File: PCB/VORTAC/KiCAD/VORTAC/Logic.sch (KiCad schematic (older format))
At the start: 46 parts, among them IC1 TMC2209-LA-T, Q1 WSD4066DN, Q3 WSD4066DN, Q4 Q_NMOS_GSD, Q5 Q_NPN_BEC, Q6 Q_PNP_BEC, Q7 Q_NMOS_GSD, Q8 Q_PMOS_GSD, U2 ADXL343

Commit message: progress
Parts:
- removed C10: 100uF/35V, symbol Device:CP
- removed IC1: TMC2209-LA-T, ToolChanger:tmc_2209_package, symbol ToolChanger:TMC2209-LA-T
- removed R16, R17: ???, symbol Device:R_Small
- removed R18, R21: 22k, symbol Device:R_Small
- removed R19: 1K, symbol Device:R_Small
- removed R20: 22K, symbol Device:R_Small
- removed U2: ADXL343, Package_LGA:LGA-14_3x5mm_P0.8mm_LayoutBorder1x6y, symbol Sensor_Motion:ADXL343
- added 10uH1, 10uH2: L, ToolChanger:L_Sunlord_MWSA0518_5.4x5.2mm, symbol Device:L
- added C10: 360pF, Capacitor_SMD:C_0603_1608Metric, symbol Device:C_Small
- added C11: 0.1uF, Capacitor_SMD:C_0603_1608Metric, symbol Device:C_Small
- added C12: 3.3nF, Capacitor_SMD:C_0603_1608Metric, symbol Device:C_Small
- added C13: 30pF, Capacitor_SMD:C_0603_1608Metric, symbol Device:C_Small
- added C14: 56pF, Capacitor_SMD:C_0603_1608Metric, symbol Device:C_Small
- added C15, C17, C19: 47uF, Capacitor_SMD:C_1206_3216Metric, symbol Device:C_Small
- added C16, C18, C20: 47uF, Capacitor_SMD:C_0805_2012Metric, symbol Device:C_Small
- added R22: 36.5k, Resistor_SMD:R_0402_1005Metric, symbol Device:R_Small
- added R23: 10k, Resistor_SMD:R_0402_1005Metric, symbol Device:R_Small
- added R24, R25: 95k, Resistor_SMD:R_0402_1005Metric, symbol Device:R_Small
- added R26, R28: 100k, Resistor_SMD:R_0402_1005Metric, symbol Device:R_Small
- added R27: 7.15k, Resistor_SMD:R_0402_1005Metric, symbol Device:R_Small
- added R29: 19.1k, Resistor_SMD:R_0402_1005Metric, symbol Device:R_Small
- added U1: TLV73333PDBV, Package_TO_SOT_SMD:SOT-23-5, symbol Regulator_Linear:TLV73333PDBV
- added U3, U4: TPS54335ADRCR, Package_SON:VSON-10-1EP_3x3mm_P0.5mm_EP1.65x2.4mm_ThermalVias, symbol ToolChanger:TPS54335ADRCR
- C1: renamed from C2; value C_Small -> 10uF 50V; footprint (none) -> Resistor_SMD:R_0603_1608Metric
- C3: value 2.2μ/6.3V -> 1uF; footprint (none) -> Capacitor_SMD:C_0603_1608Metric; LCSC (none) -> C152910
- C4: value 100n/16V -> 10uF; footprint (none) -> Capacitor_SMD:C_1206_3216Metric; LCSC (none) -> C89632
- C5: value 100n -> 10uF; footprint (none) -> Capacitor_SMD:C_1206_3216Metric; LCSC (none) -> C89632
- C6: value 22n/50V -> 0.1uF; footprint (none) -> Capacitor_SMD:C_0603_1608Metric; LCSC (none) -> C1591
- C7: value 100nV -> 0.1uF; footprint (none) -> Capacitor_SMD:C_0603_1608Metric; LCSC (none) -> C1591
- C8: value 100nV -> 1uF; footprint (none) -> Capacitor_SMD:C_0603_1608Metric; LCSC (none) -> C152910
- C9: value C_Small -> 0.1uF; footprint (none) -> Capacitor_SMD:C_0603_1608Metric; LCSC (none) -> C1591
- renumbered C1 to C2, Q8 to Q1, Q7 to Q2, Q1 to Q5, Q5 to Q7, R6 to R10, R14 to R11, R10 to R14, R11 to R15, R15 to R16, R24 to R17, R25 to R18, R26 to R19, R27 to R20, R9 to R21, R22 to R5, R23 to R6, R5 to R9
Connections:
- net TMC_VS is gone; now on net GND: C4.2, C7.2, C8.2
- net 3.3V: now also C8.1, U1.5 (OUT); no longer C5.1, C9.1
- net GND: now also C6.2, C10.2, C12.2, C13.2, C14.2, C15.2, C16.2, C17.2, C18.2, C19.2, C20.2, R24.1, R25.1, R27.2, R29.2, U1.2 (GND), U3.11 (THRM), U3.3 (GND), U3.4 (GND), U3.5 (GND), U4.11 (THRM), U4.3 (GND), U4.4 (GND), U4.5 (GND); no longer C7.1, C8.1, C9.2
- net V_IN: now also C4.1, C5.1, C6.1, C7.1, U3.1 (VIN), U4.1 (VIN)
- net 5V: now reaches C3.1
- net 5V: now also 10uH2.2, C16.1, C18.1, C20.1, R28.1, U1.1 (IN), U1.3 (EN)
- net THERM_1 renamed THERM_1_OUT
- net USBH_DRAIN renamed HOST_USB_DRAIN
- new net: R24.2, U3.10 (RT)
- new net: 10uH1.1, C9.1, U3.2 (PH)
- new net: C9.2, U3.9 (BOOT)
- new net: C13.1, R22.1
- new net: C10.1, R22.2, U3.7 (COMP)
- new net: R26.2, R27.1, U3.6 (VSENSE)
- new net: R25.2, U4.10 (RT)
- new net: 10uH2.1, C11.1, U4.2 (PH)
- new net: C11.2, U4.9 (BOOT)
- new net: C14.1, R23.1
- new net: C12.1, R23.2, U4.7 (COMP)
- new net: R28.2, R29.1, U4.6 (VSENSE)
- new net 12V: 10uH1.2, C15.1, C17.1, C19.1, R26.1
- no-connect marks 5 -> 2
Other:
- note added: "12V DC-DC Converter\n(capable of min 2A)"
- note added: "5V DC-DC Converter\n(capable of min 2.5A)"
- note added: "R2 = 0.8 / (VOUT-0.8) * 100K\nR2 = 19.047 >> 19.1K\n\nVOUT = 0.8 * R1/R2 + 0.8\nVOUT = 4.98V\n\nRT = 55300/FSW^-1.025\nRT(500 kHz) = 94.68K"
- note added: "R2 = 0.8 / (VOUT-0.8) * 100K\nR2 = 7.142 >> 7.15K\n\nVOUT = 0.8 * R1/R2 + 0.8\nVOUT =11.98V\n\nRT = 55300/FSW^-1.025\nRT(500 kHz) = 94.68K"
- note removed: "ADXL_345"
- note removed: "TMC2209"
- note removed: "TODO: This needs to be changed to ADXL345"
- note removed: "TODO: add output protection"
- moved on the sheet: C1, C2, Q3A, Q3B, Q4, Q5A, Q5B, R10, R11, R12, R13, R14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

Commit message: progress
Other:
- note added: "3.3V Linear Voltage Regulator\n(300mA for internal use only)"
- note added: "HEATER MOSFET - IRF8736TRPBF"
- note added: "THERMISTOR PASSIVES"
- note removed: "HEATER MOSFET - Infineon Technologies IRF8736TRPBF"
- moved on the sheet: 10uH1, 10uH2, C10, C11, C12, C13, C14, C15, C16, C17, C18, C19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

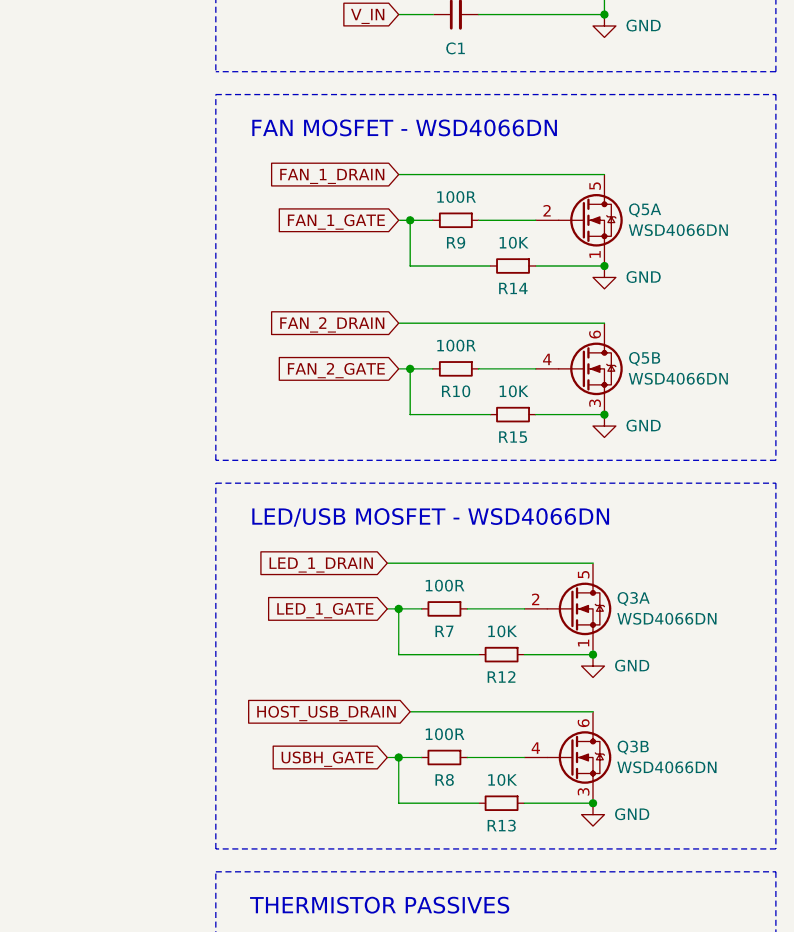
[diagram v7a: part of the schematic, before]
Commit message: Layouting & Footprints
-Improved Thermal Footprint Conductivity
-Improved Component Spacing
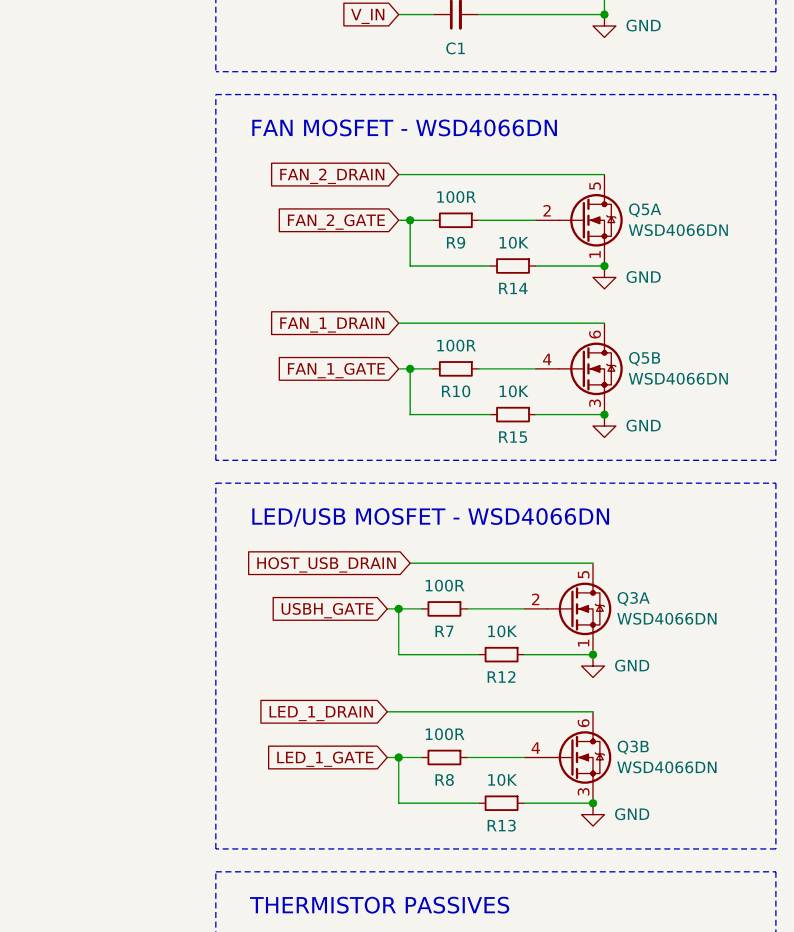
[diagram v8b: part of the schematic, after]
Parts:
- C2: footprint Capacitor_SMD:C_0402_1005Metric_Pad0.74x0.62mm_HandSolder -> Capacitor_SMD:C_0402_1005Metric
- Q3, Q5: footprint ToolChanger:WSD4066DN -> ToolChanger:WSD4066DN_ThermalPad
- U3, U4: footprint Package_SON:VSON-10-1EP_3x3mm_P0.5mm_EP1.65x2.4mm_ThermalVias -> ToolChanger:VSON-10-1EP_3x3mm_P0.5mm_EP1.65x2.4mm_ThermalVias
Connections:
- net FAN_1_DRAIN: now also Q5.6 (D2); no longer Q5.5 (D2)
- net FAN_1_GATE: now also R10.2, R15.2; no longer R14.2, R9.2
- net FAN_2_DRAIN: now also Q5.5 (D2); no longer Q5.6 (D2)
- net FAN_2_GATE: now also R14.2, R9.2; no longer R10.2, R15.2
- net HOST_USB_DRAIN: now also Q3.5 (D2); no longer Q3.6 (D2)
- net LED_1_DRAIN: now also Q3.6 (D2); no longer Q3.5 (D2)
- net LED_1_GATE: now also R13.2, R8.2; no longer R12.2, R7.2
- net USBH_GATE: now also R12.2, R7.2; no longer R13.2, R8.2
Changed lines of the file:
@@
 F 0 "Q5" H 10404 3246 50  0000 L CNN
 F 1 "WSD4066DN" H 10404 3155 50  0000 L CNN
-F 2 "ToolChanger:WSD4066DN" H 10400 3125 50  0001 L CIN
+F 2 "ToolChanger:WSD4066DN_ThermalPad" H 10400 3125 50  0001 L CIN
 F 3 "https://www.lcsc.com/product-detail/MOSFETs_Winsok-Semicon-WSD4066DN_C377861.html" H 10200 3200 50  0001 L CNN
 F 4 "C377861" H 10200 3200 50  0001 C CNN "LCSC"
@@
 	1    0    0    -1
 $EndComp
-Text GLabel 9400 3000 0    50   Input ~ 0
+Text GLabel 9400 2350 0    50   Input ~ 0
 FAN_2_DRAIN
-Text GLabel 9400 3200 0    50   Input ~ 0
+Text GLabel 9400 2550 0    50   Input ~ 0
 FAN_2_GATE
 $Comp
@@
 F 0 "Q5" H 10404 2596 50  0000 L CNN
 F 1 "WSD4066DN" H 10404 2505 50  0000 L CNN
-F 2 "ToolChanger:WSD4066DN" H 10400 2475 50  0001 L CIN
+F 2 "ToolChanger:WSD4066DN_ThermalPad" H 10400 2475 50  0001 L CIN
 F 3 "https://www.lcsc.com/product-detail/MOSFETs_Winsok-Semicon-WSD4066DN_C377861.html" H 10200 2550 50  0001 L CNN
 F 4 "C377861" H 10200 2550 50  0001 C CNN "LCSC"
@@
 	0    1    1    0
 $EndComp
-Text GLabel 9400 2550 0    50   Input ~ 0
+Text GLabel 9400 3200 0    50   Input ~ 0
 FAN_1_GATE
-Text GLabel 9400 2350 0    50   Input ~ 0
+Text GLabel 9400 3000 0    50   Input ~ 0
 FAN_1_DRAIN
 Wire Wire Line
@@
 Wire Wire Line
 	10000 3400 10300 3400
-Text GLabel 9450 4700 0    50   Input ~ 0
+Text GLabel 9450 4050 0    50   Input ~ 0
 HOST_USB_DRAIN
+Text GLabel 9350 4250 0    50   Input ~ 0
+USBH_GATE
 Text GLabel 9350 4900 0    50   Input ~ 0
-USBH_GATE
-Text GLabel 9350 4250 0    50   Input ~ 0
 LED_1_GATE
-Text GLabel 9350 4050 0    50   Input ~ 0
+Text GLabel 9350 4700 0    50   Input ~ 0
 LED_1_DRAIN
 Wire Wire Line
@@
 F 0 "Q3" H 10354 4946 50  0000 L CNN
 F 1 "WSD4066DN" H 10354 4855 50  0000 L CNN
-F 2 "ToolChanger:WSD4066DN" H 10350 4825 50  0001 L CIN
+F 2 "ToolChanger:WSD4066DN_ThermalPad" H 10350 4825 50  0001 L CIN
 F 3 "https://www.lcsc.com/product-detail/MOSFETs_Winsok-Semicon-WSD4066DN_C377861.html" H 10150 4900 50  0001 L CNN
 F 4 "C377861" H 10150 4900 50  0001 C CNN "LCSC"
@@
 F 0 "Q3" H 10354 4296 50  0000 L CNN
 F 1 "WSD4066DN" H 10354 4205 50  0000 L CNN
-F 2 "ToolChanger:WSD4066DN" H 10350 4175 50  0001 L CIN
+F 2 "ToolChanger:WSD4066DN_ThermalPad" H 10350 4175 50  0001 L CIN
 F 3 "https://www.lcsc.com/product-detail/MOSFETs_Winsok-Semicon-WSD4066DN_C377861.html" H 10150 4250 50  0001 L CNN
 F 4 "C377861" H 10150 4250 50  0001 C CNN "LCSC"
@@
 Wire Wire Line
 	9350 4250 9400 4250
-Wire Wire Line
-	9350 4050 10250 4050
 $Comp
 L Device:R_Small R7
@@
 F 0 "C2" H 10050 6100 50  0000 L CNN
 F 1 "0.1uF" H 10050 6000 50  0000 L CNN
-F 2 "Capacitor_SMD:C_0402_1005Metric_Pad0.74x0.62mm_HandSolder" H 9950 6100 50  0001 C CNN
+F 2 "Capacitor_SMD:C_0402_1005Metric" H 9950 6100 50  0001 C CNN
 F 3 "~" H 9950 6100 50  0001 C CNN
 	1    9950 6100
@@
 F 0 "U3" H 2600 2650 50  0000 C CNN
 F 1 "TPS54335ADRCR" H 2600 2800 50  0000 C CNN
-F 2 "Package_SON:VSON-10-1EP_3x3mm_P0.5mm_EP1.65x2.4mm_ThermalVias" H 2600 3250 50  0001 C CNN
+F 2 "ToolChanger:VSON-10-1EP_3x3mm_P0.5mm_EP1.65x2.4mm_ThermalVias" H 2600 3250 50  0001 C CNN
 F 3 "https://www.lcsc.com/product-detail/DC-DC-Converters_Texas-Instruments-TPS54335ADRCR_C473400.html" H 2600 3250 50  0001 C CNN
 F 4 "C473400" H 2600 3250 50  0001 C CNN "LCSC"
@@
 F 0 "U4" H 2600 4650 50  0000 C CNN
 F 1 "TPS54335ADRCR" H 2600 4800 50  0000 C CNN
-F 2 "Package_SON:VSON-10-1EP_3x3mm_P0.5mm_EP1.65x2.4mm_ThermalVias" H 2600 5250 50  0001 C CNN
+F 2 "ToolChanger:VSON-10-1EP_3x3mm_P0.5mm_EP1.65x2.4mm_ThermalVias" H 2600 5250 50  0001 C CNN
 F 3 "https://www.lcsc.com/product-detail/DC-DC-Converters_Texas-Instruments-TPS54335ADRCR_C473400.html" H 2600 5250 50  0001 C CNN
 F 4 "C473400" H 2600 5250 50  0001 C CNN "LCSC"
@@
 	1    0    0    -1
 $EndComp
-Wire Wire Line
-	9450 4700 10250 4700
 Wire Notes Line
 	600  6400 2650 6400
@@
 Text Notes 8750 5600 0    71   ~ 0
 THERMISTOR PASSIVES
+Wire Wire Line
+	9350 4700 10250 4700
+Wire Wire Line
+	9450 4050 10250 4050
 $EndSCHEMATC
